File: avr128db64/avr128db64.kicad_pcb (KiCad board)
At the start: 2 copper layers, 16 parts, among them J1 BUS1, J2 47571-0001, U1 AVR128DB64x-xPT, U2 MCP7940N-xSN, U3 74HCT138, U5 74HCT574, U6 74HCT257, U7 AS6C4008-55PCN, Y1 32kHz

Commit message: Further updates to PCB
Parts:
- removed R1: 10K, Resistor_SMD:R_0201_0603Metric
- removed U3: 74HCT138, Package_SO:SO-16_3.9x9.9mm_P1.27mm
- added C10: 0.1uf, Capacitor_SMD:C_0201_0603Metric, F.Cu at (170.5, 72.3)
- added C11: 1uf, Capacitor_SMD:C_0201_0603Metric, F.Cu at (148.7, 61.0)
- added C12: 1uf, Capacitor_SMD:C_0201_0603Metric, F.Cu at (142.7, 61.0)
- added C13: .1uf, Capacitor_SMD:C_0201_0603Metric, F.Cu at (188.3, 79.9)
- added C4: 0.1uf, Capacitor_SMD:C_0201_0603Metric, F.Cu at (160.5, 63.8)
- added C5: 0.1uf, Capacitor_SMD:C_0201_0603Metric, F.Cu at (154.3, 98.3)
- added C6: 0.1uf, Capacitor_SMD:C_0201_0603Metric, F.Cu at (144.7, 97.3)
- added C7: 0.1uf, Capacitor_SMD:C_0201_0603Metric, F.Cu at (156.5, 88.2)
- added C8: 0.1uf, Capacitor_SMD:C_0201_0603Metric, F.Cu at (124.8, 74.5)
- added C9: 0.1uf, Capacitor_SMD:C_0201_0603Metric, F.Cu at (115.3, 96.5)
- added IC1: MCP79510-I_MS, SamacSys_Parts:SOP50P490X110-10N, F.Cu at (168.3, 74.5)
- added J3: BUS3V, Connector_PinHeader_2.54mm:PinHeader_2x04_P2.54mm_Horizontal, F.Cu at (188.2, 84.5)
- added J4: SERIAL, Connector_PinHeader_2.54mm:PinHeader_2x06_P2.54mm_Horizontal, F.Cu at (188.2, 64.9)
- added R4: 1K, Resistor_SMD:R_0201_0603Metric, F.Cu at (185.6, 69.9)
- added R5: 1K, Resistor_SMD:R_0201_0603Metric, F.Cu at (185.6, 77.5)
- added R6: 1K, Resistor_SMD:R_0201_0603Metric, F.Cu at (185.6, 72.5)
- added SW1: Reset, Button_Switch_THT:SW_PUSH_6mm, F.Cu at (93.8, 75.0)
- added SW2: BANK ENA, SamacSys_Parts:JS202011SCQN, F.Cu at (116.8, 75.8)
- C3: footprint Capacitor_SMD:C_0603_1608Metric -> Capacitor_SMD:C_0201_0603Metric
- J1: value BUS1 -> BUS; footprint Connector_PinSocket_2.54mm:PinSocket_2x40_P2.54mm_Vertical -> Connector_PinHeader_2.54mm:PinHeader_2x39_P2.54mm_Horizontal
- R2: value 10K -> 4.7K
- R3: value 10K -> 1K
- U2: value MCP7940N-xSN -> MIC5504-3.3YM5; footprint Package_SO:SOIC-8_3.9x4.9mm_P1.27mm -> Package_TO_SOT_SMD:SOT-23-5
- U5: footprint Package_SO:SO-20_12.8x7.5mm_P1.27mm -> Package_SO:SOIC-20W_7.5x12.8mm_P1.27mm
- U7: footprint Package_SO:SSOP-32_11.305x20.495mm_P1.27mm -> Package_SO:TSOP-I-32_18.4x8mm_P0.5mm
- moved U6 135.8 mm to (130.5, 77.1), turned to 90 degrees
- moved U5 98.8 mm to (150.1, 74.9), turned to 90 degrees
- moved J1 96.5 mm to (190.8, 104.1), turned to -90 degrees
- moved BT1 64.6 mm to (165.7, 84.6)
- moved R3 64.6 mm to (185.6, 75.0), turned to 180 degrees
- moved U7 60.3 mm to (125.0, 91.8), turned to 180 degrees
- moved J2 57.5 mm to (167.9, 62.0), turned to 180 degrees
- moved Y1 54.7 mm to (162.8, 73.5), turned to 90 degrees
- moved U2 51.4 mm to (145.7, 62.0)
- moved R2 50.9 mm to (171.9, 73.7), turned to -90 degrees
- moved C2 39.2 mm to (160.2, 74.7), turned to 90 degrees
- moved C1 39.2 mm to (160.2, 72.2), turned to 90 degrees
- moved C3 32.7 mm to (143.0, 70.2), turned to -90 degrees
- moved U1 7.70 mm to (150.1, 91.8)
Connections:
- C1 pad 1: Net-(U2-X1) -> Net-(IC1-X1)
- C2 pad 1: Net-(U2-X2) -> Net-(IC1-X2)
- C3 pad 1: +3.3V -> +5V
- J1 pad 1: /A15 -> /USER3
- J1 pad 10: /p45 -> /RX2
- J1 pad 11: /A10 -> /D7
- J1 pad 12: /p46 -> /D15
- J1 pad 13: /A9 -> /D6
- J1 pad 14: /p47 -> /D14
- J1 pad 15: /A8 -> /D5
- J1 pad 16: /p48 -> /D13
- J1 pad 17: /A7 -> /D4
- J1 pad 18: /A23 -> /D12
- J1 pad 19: /A6 -> /D3
- J1 pad 2: /p41 -> /USER7
- J1 pad 20: /A22 -> /D11
- J1 pad 21: /A5 -> /D2
- J1 pad 22: /A21 -> /D10
- J1 pad 23: /A4 -> /D1
- J1 pad 24: /A20 -> /D9
- J1 pad 25: /A3 -> /D0
- J1 pad 26: /A19 -> /D8
- J1 pad 27: /A2 -> /~{IORQ}
- J1 pad 28: /A18 -> /~{NMI}
- J1 pad 29: /A1 -> /~{RD}
- J1 pad 3: /A14 -> /USER2
- J1 pad 30: /A17 -> /~{WAIT}
- J1 pad 31: /A0 -> /~{WR}
- J1 pad 32: /A16 -> /~{BUSRQ}
- J1 pad 33: GND -> /~{MREQ}
- J1 pad 34: GND -> /~{HALT}
- J1 pad 35: +5V -> /~{INT}
- J1 pad 36: +5V -> /~{BUSACK}
- J1 pad 37: /~{M1} -> /CLK
- J1 pad 38: /~{RFSH} -> /CLOCK2
- J1 pad 4: /p42 -> /USER6
- J1 pad 41: /CLK -> /~{M1}
- J1 pad 42: /CLOCK2 -> /~{RFSH}
- J1 pad 43: /~{INT} -> +5V
- J1 pad 44: /~{BUSACK} -> +5V
- J1 pad 45: /~{MREQ} -> GND
- J1 pad 46: /~{HALT} -> GND
- J1 pad 47: /~{WR} -> /A0
- J1 pad 48: /~{BUSRQ} -> /A16
- J1 pad 49: /~{RD} -> /A1
- J1 pad 5: /A13 -> /USER1
- J1 pad 50: /~{WAIT} -> /A17
- J1 pad 51: /~{IORQ} -> /A2
- J1 pad 52: /~{NMI} -> /A18
- J1 pad 53: /D0 -> /A3
- J1 pad 54: /D8 -> /A19
- J1 pad 55: /D1 -> /A4
- J1 pad 56: /D9 -> /A20
- J1 pad 57: /D2 -> /A5
- J1 pad 58: /D10 -> /A21
- J1 pad 59: /D3 -> /A6
- J1 pad 6: /p43 -> /USER5
- J1 pad 60: /D11 -> /A22
- J1 pad 61: /D4 -> /A7
- J1 pad 62: /D12 -> /A23
- J1 pad 63: /D5 -> /A8
- J1 pad 64: /D13 -> /p48
- J1 pad 65: /D6 -> /A9
- J1 pad 66: /D14 -> /p47
- J1 pad 67: /D7 -> /A10
- J1 pad 68: /D15 -> /p46
- J1 pad 69: /TX -> /A11
- J1 pad 7: /A12 -> /RX
- J1 pad 70: /RX2 -> /p45
- J1 pad 71: /RX -> /A12
- J1 pad 72: /TX2 -> /p44
- J1 pad 73: /USER1 -> /A13
- J1 pad 74: /USER5 -> /p43
- J1 pad 75: /USER2 -> /A14
- J1 pad 76: /USER6 -> /p42
- J1 pad 77: /USER3 -> /A15B
- J1 pad 78: /USER7 -> /p41
- J1 pad 8: /p44 -> /TX2
- J1 pad 9: /A11 -> /TX
- J2 pad P2: /SDCS -> /~{SDCS}
- R2 pad 1: /SCL5V -> +3.3V
- R2 pad 2: +5V -> /~{INT3V}
- R3 pad 1: /MFP -> Net-(J4-Pin_9)
- R3 pad 2: +5V -> /TX
- U1 pad 1: /~{BUSRQ} -> /~{RST}
- U1 pad 10: /D2 -> /~{RD}
- U1 pad 11: /D3 -> /~{WAIT}
- U1 pad 12: /D4 -> /TX2
- U1 pad 13: /D5 -> /RX2
- U1 pad 14: /D6 -> /~{RFSH}
- U1 pad 15: /D7 -> /~{NMI}
- U1 pad 16: /TX3V -> /RX3V
- U1 pad 17: /RX3V -> /TX3V
- U1 pad 18: /SDA3V -> /~{INT3V}
- U1 pad 19: /SCL3V -> /~{SDCS}
- U1 pad 2: /~{RD} -> /CLK
- U1 pad 25: /SDCS -> /~{RTCCS}
- U1 pad 26: /A8 -> /D0
- U1 pad 27: /A9 -> /D1
- U1 pad 28: /A10 -> /D2
- U1 pad 29: /A11 -> /D3
- U1 pad 3: /~{WAIT} -> /~{BUSACK}
- U1 pad 30: /A12 -> /D4
- U1 pad 31: /A13 -> /D5
- U1 pad 32: /A14 -> /D6
- U1 pad 33: /A15 -> /D7
- U1 pad 36: /A0 -> /A8
- U1 pad 37: /A1 -> /A9
- U1 pad 38: /A2 -> /A10
- U1 pad 39: /A3 -> /A11
- U1 pad 4: /~{IORQ} -> /~{INT}
- U1 pad 40: /A4 -> /A12
- U1 pad 41: /A5 -> /A13
- U1 pad 42: /A6 -> /A14
- U1 pad 43: /A7 -> /A15
- U1 pad 44: unconnected-(U1-XTAL32K1/PF0-Pad44) -> /TX
- U1 pad 45: unconnected-(U1-XTAL32K2/PF1-Pad45) -> /RX
- U1 pad 46: /SDA5V -> /A16
- U1 pad 47: /SCL5V -> /A17
- U1 pad 48: /MFP -> /A18
- U1 pad 49: unconnected-(U1-PF5-Pad49) -> /BCLK
- U1 pad 5: /~{NMI} -> /~{HALT}
- U1 pad 50: unconnected-(U1-~{RESET}/PF6-Pad50) -> Net-(U1-~{RESET}/PF6)
- U1 pad 52: unconnected-(U1-PG0-Pad52) -> /~{WR}
- U1 pad 53: unconnected-(U1-PG1-Pad53) -> /~{M1}
- U1 pad 54: /~{M1} -> /A0
- U1 pad 55: /~{RFSH} -> /A1
- U1 pad 58: /~{RST} -> /A2
- U1 pad 59: /CLK -> /A3
- U1 pad 60: /~{INT} -> /A4
- U1 pad 61: /~{BUSACK} -> /A5
- U1 pad 62: /~{MREQ} -> /A6
- U1 pad 63: /~{HALT} -> /A7
- U1 pad 64: /~{WR} -> /~{IORQ}
- U1 pad 8: /D0 -> /~{MREQ}
- U1 pad 9: /D1 -> /~{BUSRQ}
- U2 pad 1: Net-(U2-X1) -> +5V
- U2 pad 2: Net-(U2-X2) -> GND
- U2 pad 3: Net-(BT1-+) -> +5V
- U2 pad 4: GND -> unconnected-(U2-NC-Pad4)
- U2 pad 5: /SDA5V -> +3.3V
- U5 pad 11: unconnected-(U5-Cp-Pad11) -> /BCLK
- U5 pad 20: VCC -> +5V
- U6 pad 1: /A15 -> /A15B
- U6 pad 12: /B17 -> /A17
- U6 pad 15: GND -> /~{BANK}
- U6 pad 16: VCC -> +5V
- U6 pad 4: /B15 -> /A15
- U6 pad 7: /B16 -> /A16
- U6 pad 9: /B18 -> /A18
- U7 pad 1: /B18 -> /A18
- U7 pad 2: /B16 -> /A16
- U7 pad 30: /B17 -> /A17
- U7 pad 31: /B15 -> /A15
- U7 pad 32: VCC -> +5V
- Y1 pad 1: Net-(U2-X2) -> Net-(IC1-X2)
- Y1 pad 2: Net-(U2-X1) -> Net-(IC1-X1)
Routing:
- net +5V: track 0.00 -> 154.0 mm, vias 0 -> 6
- net /D6: track 0.00 -> 81.6 mm, vias 0 -> 2
- net /D7: track 0.00 -> 80.5 mm
- net /D5: track 0.00 -> 79.0 mm, vias 0 -> 2
- net /D4: track 0.00 -> 76.4 mm, vias 0 -> 2
- net /D3: track 0.00 -> 74.4 mm, vias 0 -> 2
- net /A12: track 0.00 -> 71.9 mm, vias 0 -> 5
- net /A14: track 0.00 -> 69.8 mm, vias 0 -> 4
- net /A13: track 0.00 -> 60.9 mm, vias 0 -> 1
- net /D0: track 0.00 -> 58.9 mm, vias 0 -> 2
- net /D1: track 0.00 -> 58.3 mm, vias 0 -> 2
- net /D2: track 0.00 -> 58.3 mm, vias 0 -> 4
- net /A11: track 0.00 -> 53.6 mm, vias 0 -> 1
- net /A10: track 0.00 -> 52.3 mm, vias 0 -> 1
- net /A9: track 0.00 -> 52.1 mm, vias 0 -> 3
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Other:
- board outline added: 99.8 x 49.9 mm

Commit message: Additional traces
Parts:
- removed IC1: MCP79510-I_MS, SamacSys_Parts:SOP50P490X110-10N
- added C14: 0.1uf, Capacitor_SMD:C_0402_1005Metric, F.Cu at (153.1, 84.1)
- added R1: 4.7K, Resistor_SMD:R_0402_1005Metric, F.Cu at (176.1, 84.2)
- added SW3: SW_DIP_x06, Button_Switch_THT:SW_DIP_SPSTx06_Slide_9.78x17.42mm_W7.62mm_P2.54mm, F.Cu at (183.1, 86.8)
- added SW4: SW_DIP_x04, Button_Switch_THT:SW_DIP_SPSTx04_Slide_9.78x12.34mm_W7.62mm_P2.54mm, F.Cu at (170.4, 91.9)
- added U3: MCP7940N-xST, Package_SO:TSSOP-8_3x3mm_P0.65mm, F.Cu at (172.1, 84.3)
- BT1: footprint Battery:BatteryHolder_Keystone_500 -> Battery:BatteryHolder_Keystone_3000_1x12mm
- C1, C10, C11, C12, C2, C3, C4, C5, C6, C7, C8, C9: footprint Capacitor_SMD:C_0201_0603Metric -> Capacitor_SMD:C_0402_1005Metric
- C13: value .1uf -> 0.1uf; footprint Capacitor_SMD:C_0201_0603Metric -> Capacitor_SMD:C_0402_1005Metric
- J3: value BUS3V -> UEXT; footprint Connector_PinHeader_2.54mm:PinHeader_2x04_P2.54mm_Horizontal -> Connector_PinHeader_2.54mm:PinHeader_2x05_P2.54mm_Vertical
- R2, R3, R4, R5, R6: footprint Resistor_SMD:R_0201_0603Metric -> Resistor_SMD:R_0402_1005Metric
- moved BT1 66.6 mm to (99.4, 91.5), turned to -90 degrees
- moved J3 28.5 mm to (170.1, 62.6), turned to 90 degrees
- moved R2 12.3 mm to (176.1, 85.3), turned to 180 degrees
- moved C4 11.2 mm to (149.5, 61.5)
- moved C2 11.2 mm to (164.6, 85.0), turned to -90 degrees
- moved Y1 10.7 mm to (167.1, 83.3)
- moved J2 10.7 mm to (157.2, 62.0)
- moved C1 10.3 mm to (164.6, 81.6)
- moved C10 10.3 mm to (174.1, 81.9)
- moved C6 5.88 mm to (142.5, 91.8), turned to 180 degrees
- moved C7 5.75 mm to (157.8, 93.8), turned to 0 degrees
- moved C5 5.36 mm to (149.1, 99.5)
- moved C8 4.46 mm to (124.6, 70.1)
- moved U6 4.46 mm to (130.5, 72.6)
- moved SW2 1.81 mm to (116.8, 74.0)
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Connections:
- C13 pad 1: /~{AVRRST} -> /AVRRST
- J1 pad 10: /RX2 -> /BTX2
- J1 pad 7: /RX -> /BRX
- J1 pad 8: /TX2 -> /BRX2
- J1 pad 9: /TX -> /BTX
- J3 pad 1: GND -> +3.3V
- J3 pad 2: /~{INT3V} -> GND
- J3 pad 3: /SCK -> /TX3
- J3 pad 4: /TX/~{CS2} -> /RX3
- J3 pad 5: /MISO -> /SCL
- J3 pad 6: /RX/~{CS1} -> /SDA
- J3 pad 7: /MOSI -> /MISO
- J3 pad 8: +3.3V -> /MOSI
- R2 pad 2: /~{INT3V} -> /SCL
- SW1 pad 2: Net-(U1-~{RESET}/PF6) -> /AVRRST
- U1 pad 16: /RX3V -> /RX3
- U1 pad 17: /TX3V -> /TX3
- U1 pad 18: /~{INT3V} -> /SDA
- U1 pad 19: /~{SDCS} -> /SCL
- U1 pad 25: /~{RTCCS} -> /~{SDCS}
- U1 pad 50: Net-(U1-~{RESET}/PF6) -> /AVRRST
- U2 pad 3: +5V -> /AVRRST
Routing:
- net Net-(BT1-+): track 0.00 -> 136.4 mm, vias 0 -> 2
- net /SDA: track 0.00 -> 104.1 mm
- net /~{SDCS}: track 0.00 -> 64.0 mm, vias 0 -> 1
- net /MOSI: track 0.00 -> 62.6 mm, vias 0 -> 3
- net /SCK: track 0.00 -> 59.8 mm, vias 0 -> 1
- net /A17: track 29.2 -> 87.0 mm, vias 1 -> 3
- net /AVRRST: track 0.00 -> 57.1 mm
- net /MISO: track 0.00 -> 56.7 mm, vias 0 -> 1
- net /TX2: track 0.00 -> 54.2 mm, vias 0 -> 2
- net /SCL: track 0.00 -> 53.3 mm
- net /RX2: track 0.00 -> 53.1 mm, vias 0 -> 2
- net /~{WR}: track 0.00 -> 52.6 mm, vias 0 -> 2
- net /RX3: track 0.00 -> 50.4 mm, vias 0 -> 2
- net /~{RD}: track 9.88 -> 56.9 mm, vias 0 -> 2
- net /~{MREQ}: track 10.8 -> 57.4 mm, vias 0 -> 2
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- added copper zone on B.Cu, net GND
- added copper zone on F.Cu, net GND

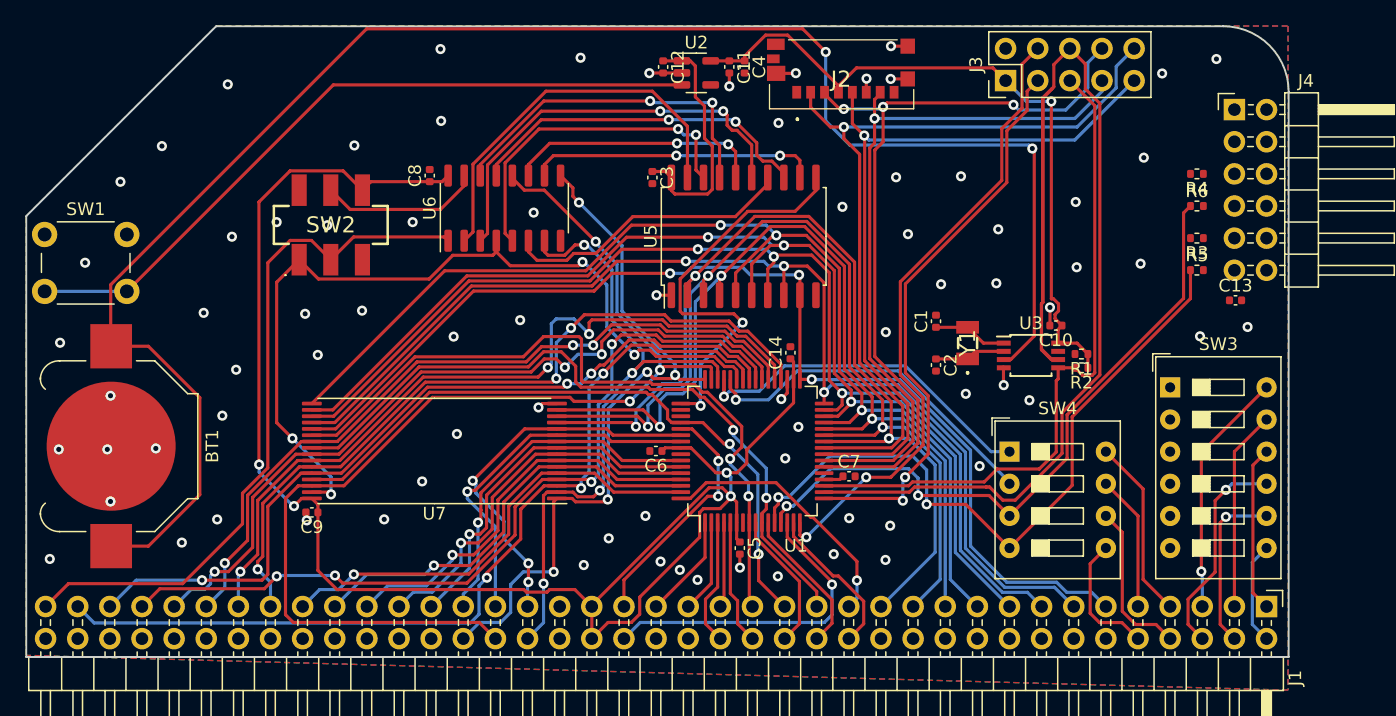
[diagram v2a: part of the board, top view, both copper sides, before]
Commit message: Finish routing all signals and fix DRC errors
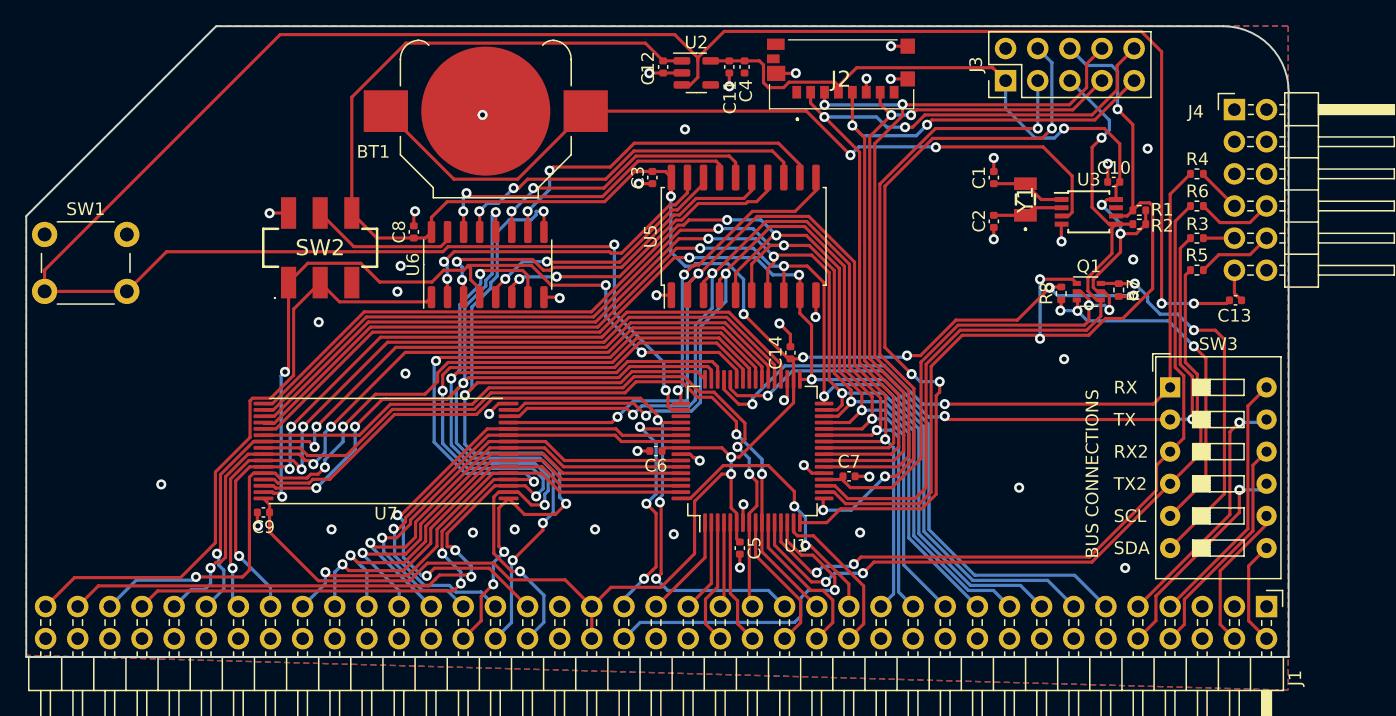
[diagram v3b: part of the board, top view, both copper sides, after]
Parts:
- removed SW4: SW_DIP_x04, Button_Switch_THT:SW_DIP_SPSTx04_Slide_9.78x12.34mm_W7.62mm_P2.54mm
- added Q1: FDG6335N, Package_TO_SOT_SMD:SOT-363_SC-70-6, F.Cu at (176.7, 79.2)
- added R7: 4.7K, Resistor_SMD:R_0402_1005Metric, F.Cu at (179.1, 79.1)
- added R8: 4.7K, Resistor_SMD:R_0402_1005Metric, F.Cu at (174.5, 79.4)
- moved BT1 39.7 mm to (129.0, 65.0), turned to 180 degrees
- moved C1 12.2 mm to (169.2, 70.2)
- moved C10 12.2 mm to (178.7, 70.6)
- moved R1 12.2 mm to (180.7, 72.8)
- moved U3 12.2 mm to (176.7, 72.9)
- moved Y1 12.2 mm to (171.7, 72.0)
- moved C2 12.2 mm to (169.2, 73.7)
- moved R2 12.2 mm to (180.7, 73.9)
- moved U6 4.65 mm to (129.2, 77.1)
- moved C8 4.63 mm to (123.3, 74.5)
- moved C9 3.82 mm to (111.5, 96.7)
- moved U7 3.82 mm to (121.1, 91.8)
- moved SW2 1.99 mm to (115.9, 75.8)
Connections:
- net /BCLK renamed /BCK
- net /RX3 renamed /~{CS2}/RX3
- J3 pad 3: /TX3 -> /~{CS1}/TX3
- J4 pad 5: /VCCs -> unconnected-(J4-Pin_5-Pad5)
- SW3 pad 1: /SDA -> /RX
- SW3 pad 10: /USER3 -> /BRX2
- SW3 pad 11: /USER2 -> /BTX
- SW3 pad 12: /USER1 -> /BRX
- SW3 pad 2: /SCL -> /TX
- SW3 pad 3: /TX3 -> /RX2
- SW3 pad 4: /SCK -> /TX2
- SW3 pad 5: /MISO -> /SCL5V
- SW3 pad 6: /MOSI -> /SDA5V
- SW3 pad 9: /USER5 -> /BTX2
- U1 pad 17: /TX3 -> /~{CS1}/TX3
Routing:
- net /AVRRST: track 57.1 -> 190.7 mm, vias 0 -> 4
- net Net-(BT1-+): track 136.4 -> 65.2 mm
- net /~{CS1}/TX3: track 0.00 -> 50.7 mm, vias 0 -> 3
- net /TX3: track 45.4 -> 0.00 mm, vias 2 -> 0
- net +5V: track 151.3 -> 194.6 mm, vias 4 -> 8
- net +3.3V: track 57.2 -> 95.9 mm, vias 1 -> 5
- net /SDA: track 104.1 -> 73.2 mm, vias 0 -> 3
- net /SDA5V: track 0.00 -> 30.1 mm, vias 0 -> 2
- net /RX: track 27.8 -> 57.4 mm, vias 1 -> 2
- net /SCL5V: track 0.00 -> 28.4 mm, vias 0 -> 3
- net /TX: track 28.2 -> 55.0 mm, vias 1 -> 3
- net /A16: track 52.4 -> 72.5 mm
- net /USER1: track 19.5 -> 0.00 mm, vias 1 -> 0
- net GND: track 18.3 -> 37.0 mm, vias 79 -> 44
- net /A14: track 71.2 -> 88.1 mm, vias 3 -> 4
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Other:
- board text added: "BUS CONNECTIONS"
- board text added: "RX"
- board text added: "RX2"
- board text added: "SCL"
- board text added: "SDA"
- board text added: "TX"
- board text added: "TX2"
